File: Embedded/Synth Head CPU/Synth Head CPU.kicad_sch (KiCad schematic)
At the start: 17 parts, among them J1 10171746-00021LF, J2 JST [C], U5 FFC [G], U6 FFC [M], U7 FFC [K], U8 NEO-M8M

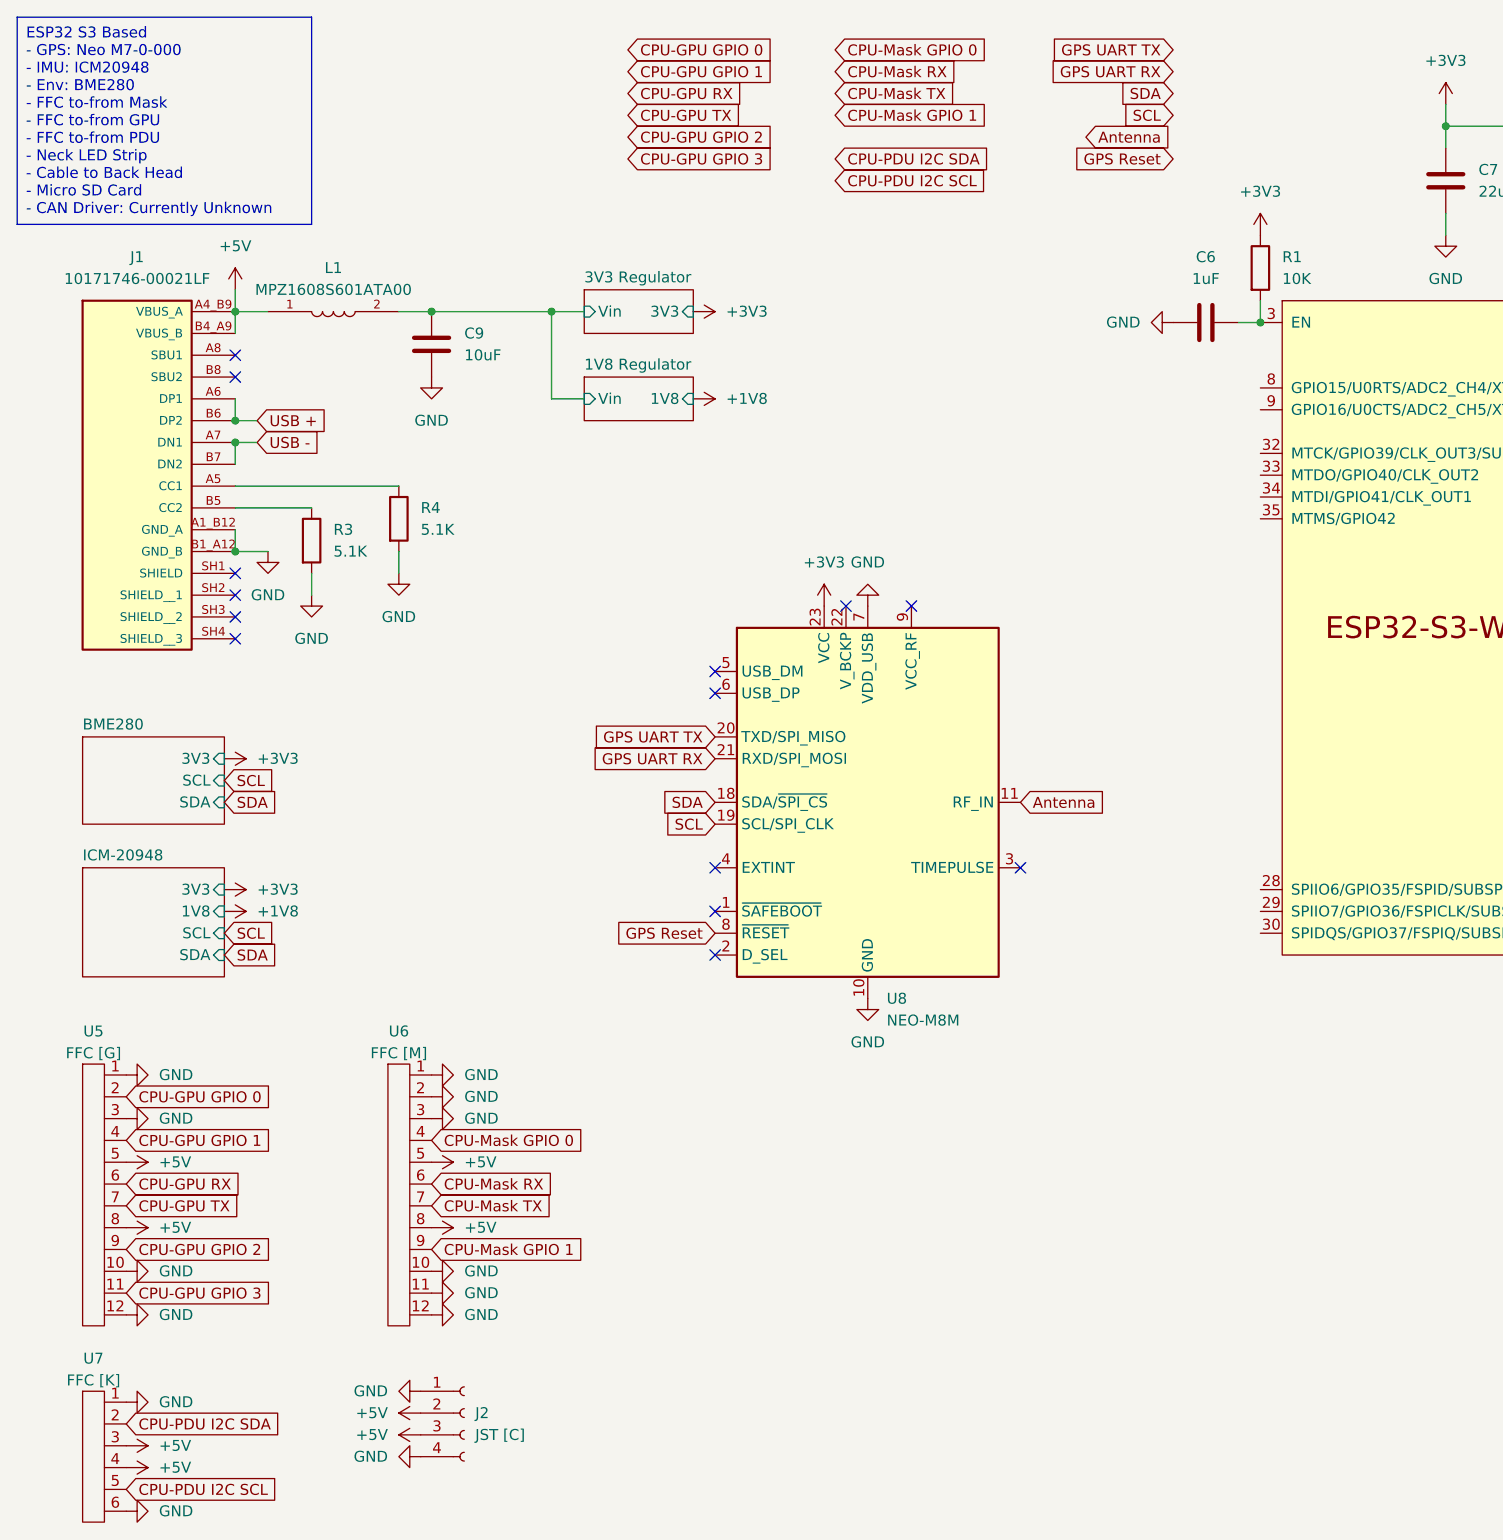
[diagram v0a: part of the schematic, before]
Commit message: Added I2C GPIO Expansion to GPU & Some Pin Position Updates
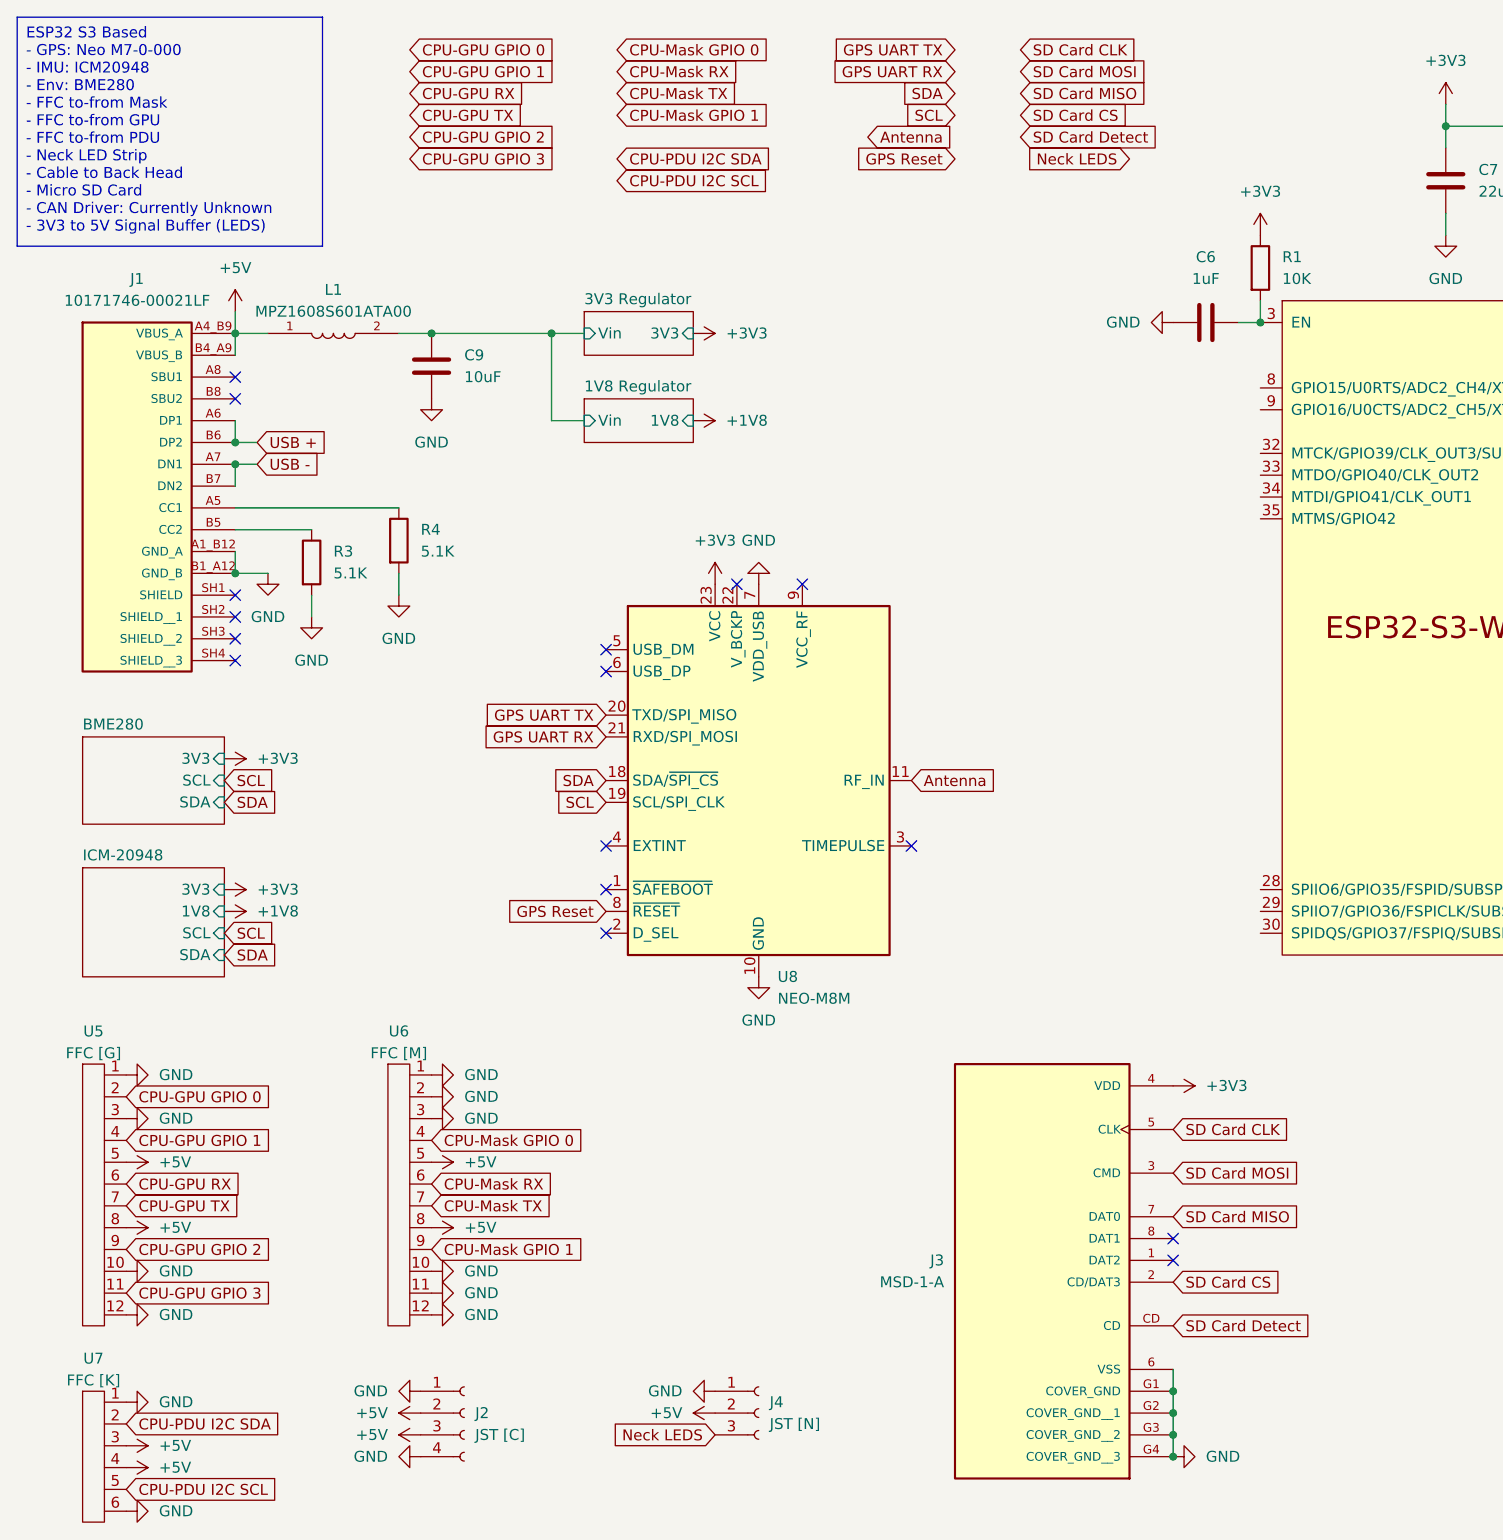
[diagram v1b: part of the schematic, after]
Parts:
- added J3: MSD-1-A, MSD-1-A:CUI_MSD-1-A, symbol MicroSD_MSD_1_A:MSD-1-A
- added J4: JST [N], symbol Connector:Conn_01x03_Socket
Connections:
- net +3V3: now also J3.4 (VDD)
- net +5V: now also J4.2 (Pin_2)
- net GND: now also J3.6 (VSS), J3.G1 (COVER_GND), J3.G2 (COVER_GND__1), J3.G3 (COVER_GND__2), J3.G4 (COVER_GND__3), J4.1 (Pin_1)
- new net Neck LEDS: J4.3 (Pin_3)
- new net SD Card CLK: J3.5 (CLK)
- new net SD Card CS: J3.2 (CD/DAT3)
- new net SD Card Detect: J3.CD
- new net SD Card MISO: J3.7 (DAT0)
- new net SD Card MOSI: J3.3 (CMD)
- no-connect marks 20 -> 22
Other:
- moved on the sheet: C9, J1, L1, R3, R4, U8

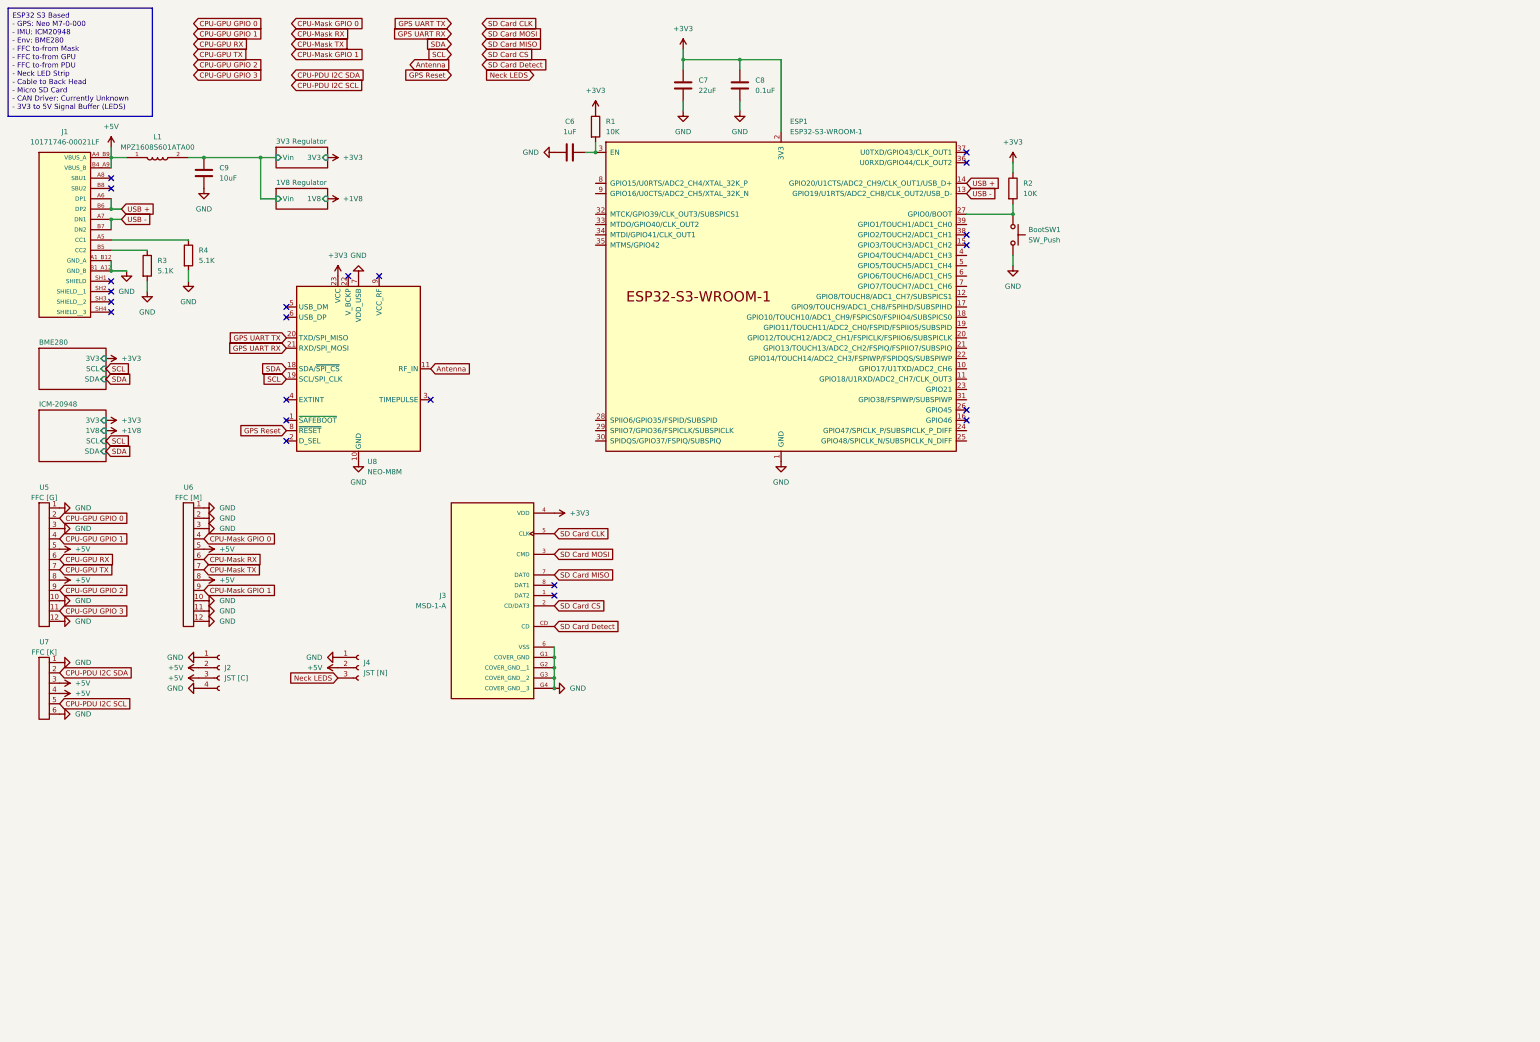
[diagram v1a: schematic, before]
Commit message: Added Voltage Buffer & Modified Sheet Hierarchy
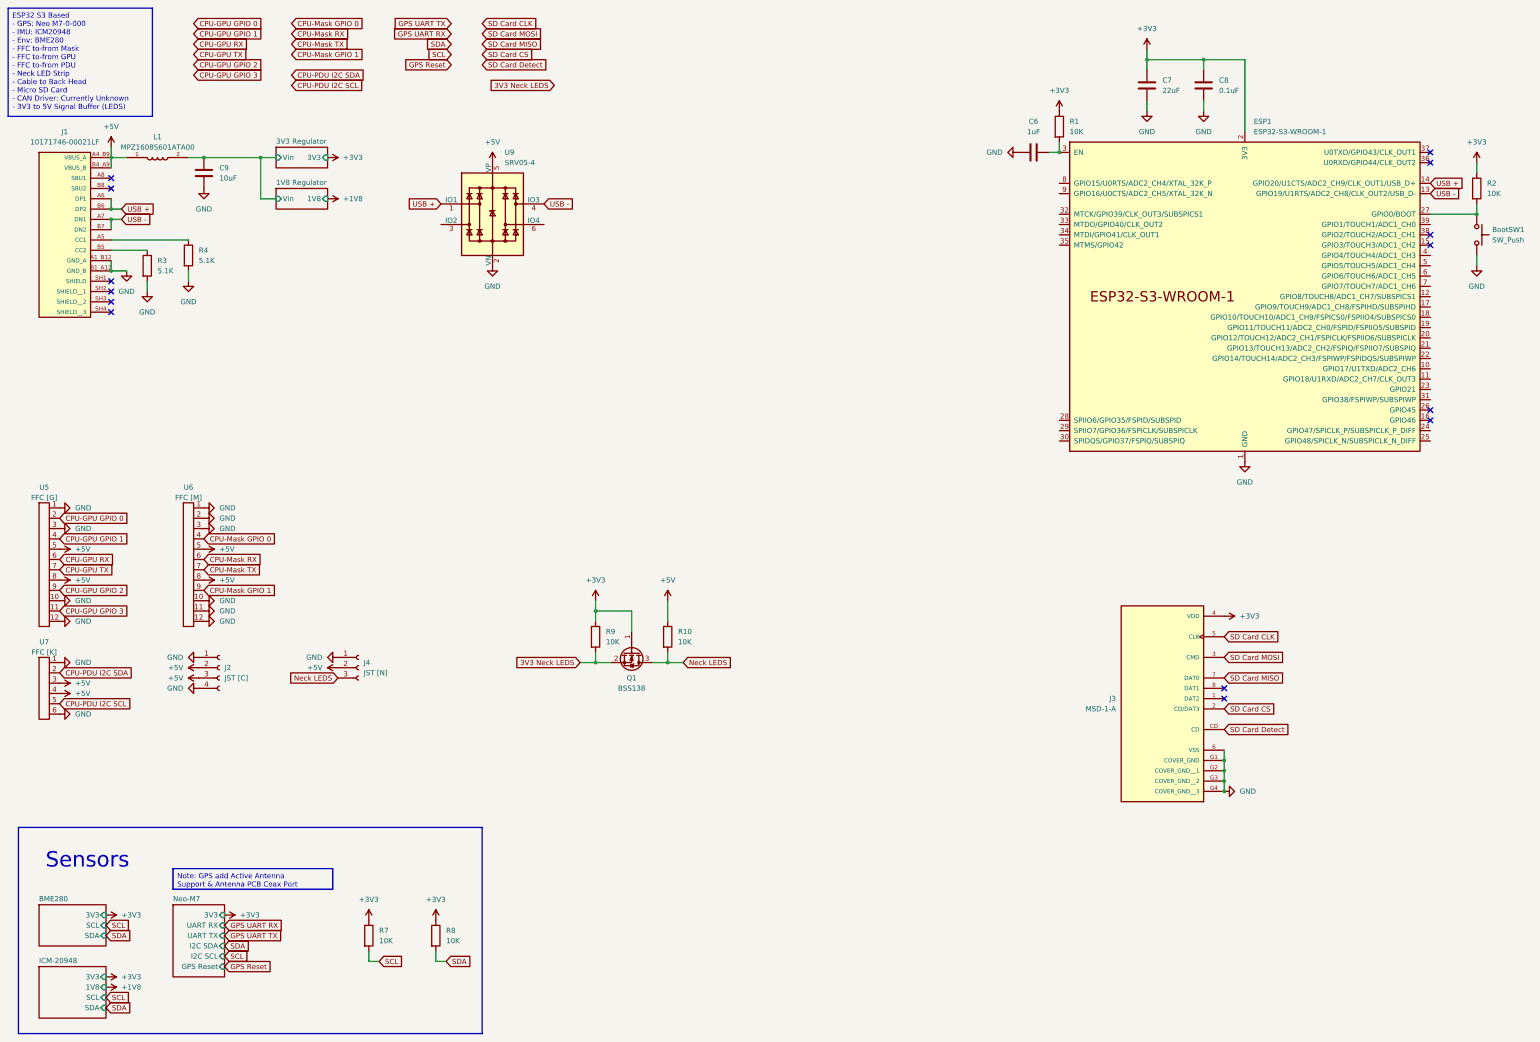
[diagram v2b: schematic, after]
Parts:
- removed U8: NEO-M8M, RF_GPS:ublox_NEO, symbol RF_GPS:NEO-M8M
- added Q1: BSS138, Package_TO_SOT_SMD:SOT-23, symbol Transistor_FET:BSS138
- added R10, R7, R8, R9: 10K, symbol Device:R
- added U9: SRV05-4, Package_TO_SOT_SMD:SOT-23-6, symbol Power_Protection:SRV05-4
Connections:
- net +3V3: now also Q1.1 (G), R7.1, R8.1, R9.1
- net +5V: now also R10.1, U9.5 (VP)
- net GND: now also U9.2 (VN)
- net Neck LEDS: now also Q1.3 (D), R10.2
- net SCL: now also R7.2
- net SDA: now also R8.2
- net USB +: now also U9.1 (IO1)
- net USB -: now also U9.4 (IO3)
- new net 3V3 Neck LEDS: Q1.2 (S), R9.2
- no-connect marks 22 -> 14
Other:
- added sheet Neo-M7 (Neo-M7.kicad_sch)
- note added: "Sensors"
- moved on the sheet: BootSW1, C6, C7, C8, ESP1, J3, R1, R2
